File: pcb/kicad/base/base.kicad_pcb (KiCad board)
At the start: 2 copper layers, 45 parts, among them P1 J-Link SWD, P2 SMA, P3 Power Source, P4 USB Micro B, Q1 IRLML2502, U1 SAMB11G18A-edit, U2 XBee-PRO_900HP, Y1 32.768kHz, Y2 26MHz

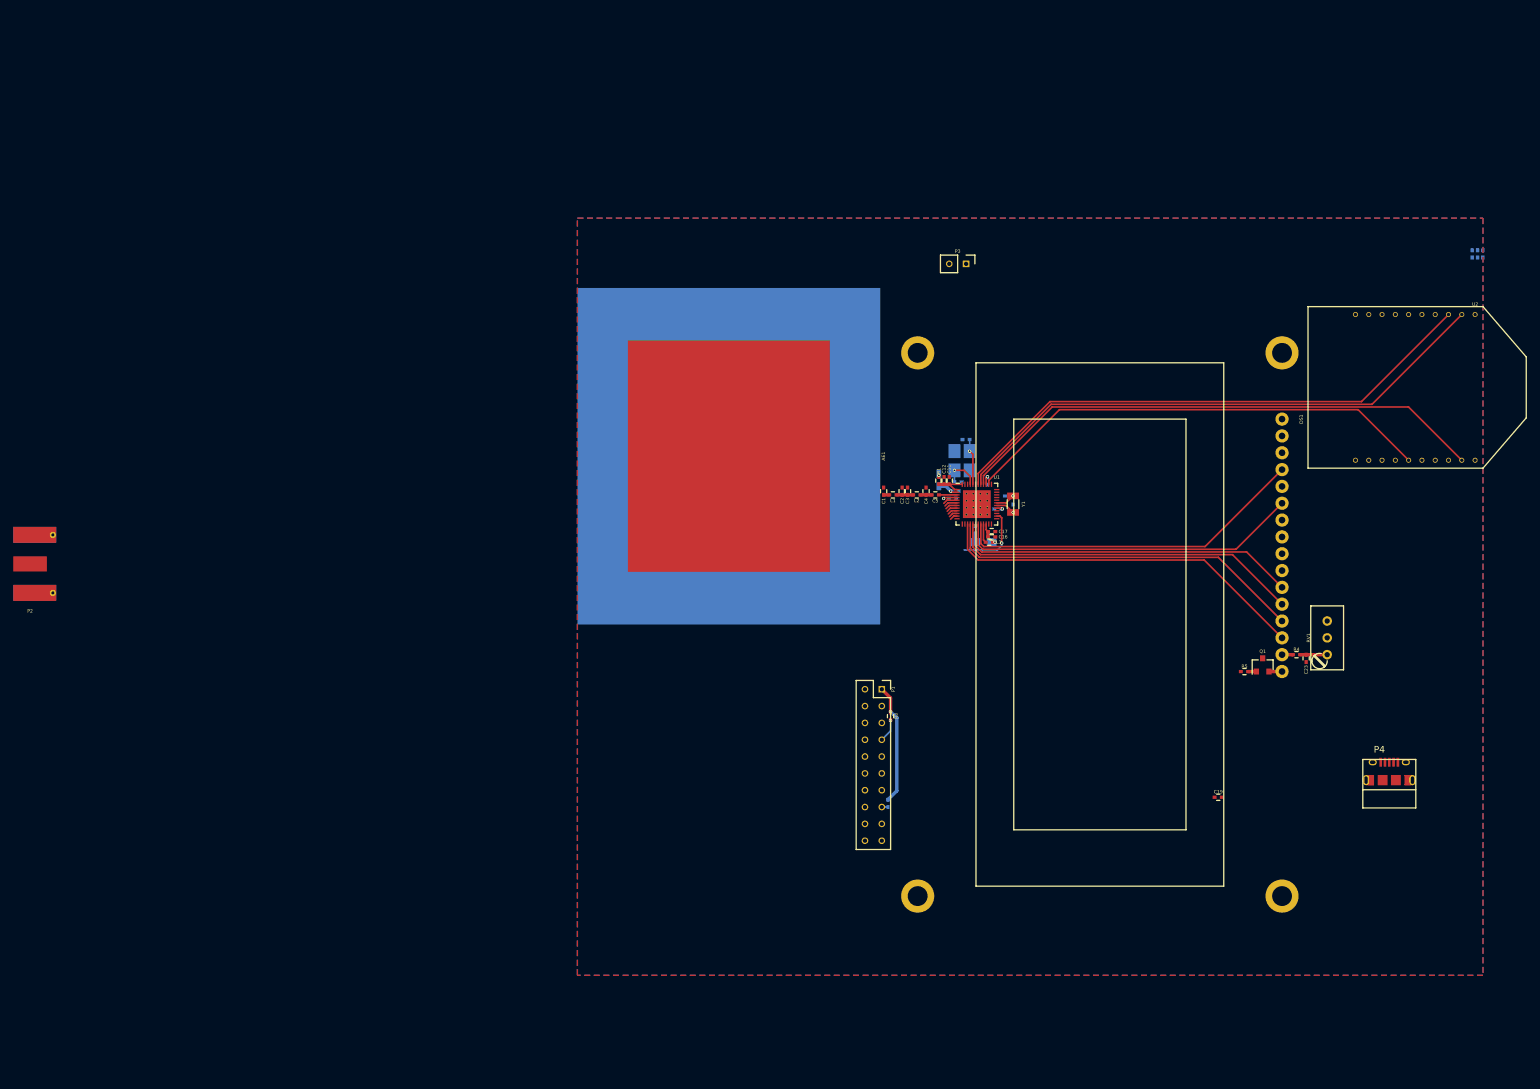
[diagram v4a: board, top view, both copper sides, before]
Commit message: Update display and XBee position once more
GPIO pins were rearranged to achieve a tighter fit on the available
components. Patch antenna is now replaced with SMA connector for first
prototype. Buttons will be simulated with a pin header short. Audio
speaker is planned to go below the display, perhpas on the side of the
housing.
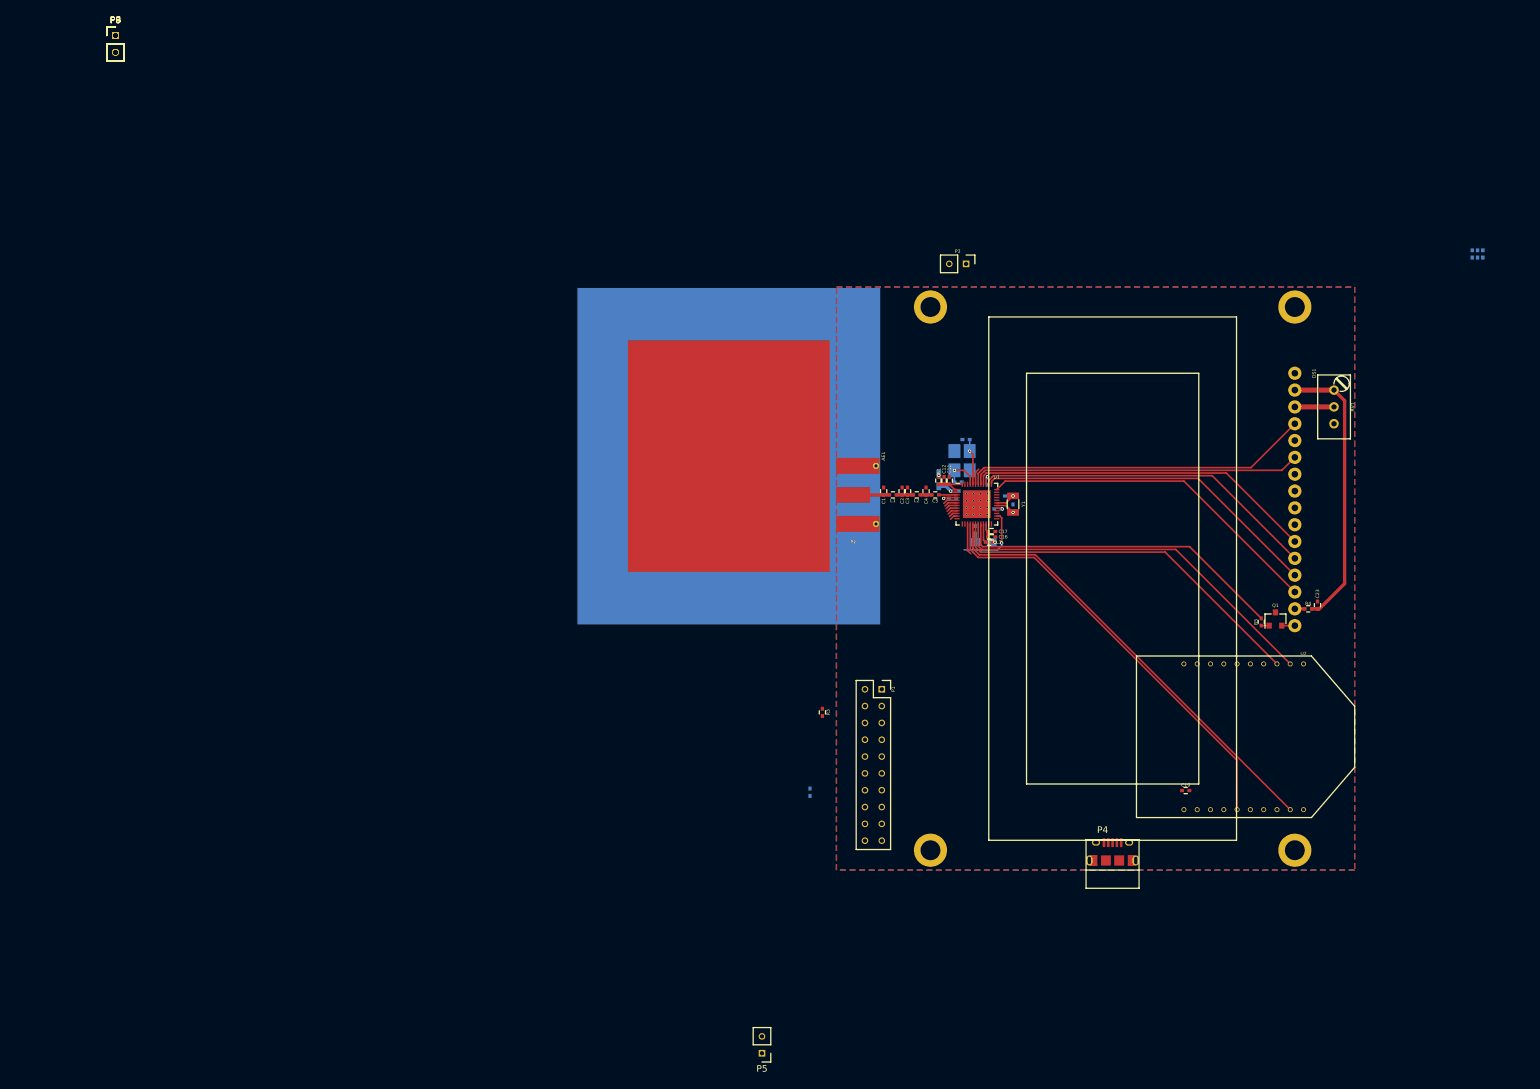
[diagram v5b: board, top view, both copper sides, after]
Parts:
- added P5: Button, Misc:Socket_Strip_Straight_1x02_Pitch2.54mm_Drill0.64mm, F.Cu at (97.6, 153.6)
- added P6, P7, P8, P9: Button, Misc:Socket_Strip_Straight_1x02_Pitch2.54mm_Drill0.64mm, F.Cu at (0.00, 0.00)
- moved P2 124.7 mm to (113.1, 69.3)
- moved U2 58.8 mm to (176.9, 105.9)
- moved P4 43.5 mm to (150.5, 124.5)
- moved RV1 40.0 mm to (183.9, 53.5), turned to 90 degrees
- moved R2 11.9 mm to (104.8, 114.2)
- moved R3 10.3 mm to (106.7, 102.2)
- moved C23 8.21 mm to (181.4, 86.0), turned to 270 degrees
- moved R5 7.91 mm to (172.9, 88.5), turned to 270 degrees
- moved Q1 7.20 mm to (175.1, 88.1)
- moved DS1 7.19 mm to (150.5, 82.0)
- moved R4 7.15 mm to (180.0, 86.5)
- moved C19 5.02 mm to (161.5, 114.0)
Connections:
- AE1 pad 1: /SIG_2.4G -> Net-(AE1-Pad1)
- P2 pad 1: Net-(P2-Pad1) -> /SIG_2.4G
- R5 pad 1: /base-display/BRIGHT -> /DISP_BRIGHT
- U1 pad 10: Net-(U1-Pad10) -> /BTN_UP
- U1 pad 11: Net-(U1-Pad11) -> /BTN_RIGHT
- U1 pad 12: Net-(U1-Pad12) -> /BTN_HELP
- U1 pad 13: Net-(U1-Pad13) -> /Data-
- U1 pad 14: /DISP_CTRST -> /Data+
- U1 pad 15: /DISP_B3 -> /AUDIO_SIG
- U1 pad 16: /DISP_B2 -> /UART_RTS
- U1 pad 17: /DISP_B1 -> /UART_CTS
- U1 pad 18: /DISP_B0 -> /UART_TX
- U1 pad 19: /DISP_E -> /UART_RX
- U1 pad 20: /DISP_REG -> /DISP_BRIGHT
- U1 pad 24: GND -> Net-(U1-Pad24)
- U1 pad 25: GND -> Net-(U1-Pad25)
- U1 pad 27: GND -> Net-(U1-Pad27)
- U1 pad 28: GND -> Net-(U1-Pad28)
- U1 pad 33: GND -> Net-(U1-Pad33)
- U1 pad 36: GND -> /DISP_B3
- U1 pad 37: GND -> /DISP_B2
- U1 pad 38: /UART_RTS -> /DISP_B1
- U1 pad 40: /UART_CTS -> /DISP_B0
- U1 pad 41: /UART_RX -> /DISP_E
- U1 pad 42: /UART_TX -> /DISP_REG
- U1 pad 43: GND -> /DISP_CTRST
- U1 pad 7: /Data- -> Net-(U1-Pad7)
- U1 pad 8: /Data+ -> /BTN_LEFT
- U1 pad 9: Net-(U1-Pad9) -> /BTN_DOWN
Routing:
- net /DISP_BRIGHT: track 0.00 -> 50.1 mm
- net /+5V: track 4.09 -> 42.3 mm
- net /UART_RX: track 84.1 -> 57.8 mm
- net /UART_TX: track 82.6 -> 56.3 mm
- net /+3.3V: track 21.5 -> 3.28 mm, vias 2 -> 1
- net /UART_CTS: track 81.1 -> 67.9 mm
- net /UART_RTS: track 71.5 -> 64.7 mm
- net Net-(DS1-Pad3): track 0.00 -> 5.91 mm
- net /AUDIO_SIG: track 0.00 -> 4.66 mm
- net /SIG_2.4G: track 0.85 -> 5.44 mm
- net /DISP_B3: track 56.8 -> 52.5 mm
- net /SWDIO: track 5.45 -> 2.01 mm, vias 1 -> 0
- net /DISP_B2: track 55.3 -> 52.5 mm
- net /DISP_CTRST: track 0.00 -> 2.46 mm
- net /DISP_E: track 52.1 -> 50.0 mm
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
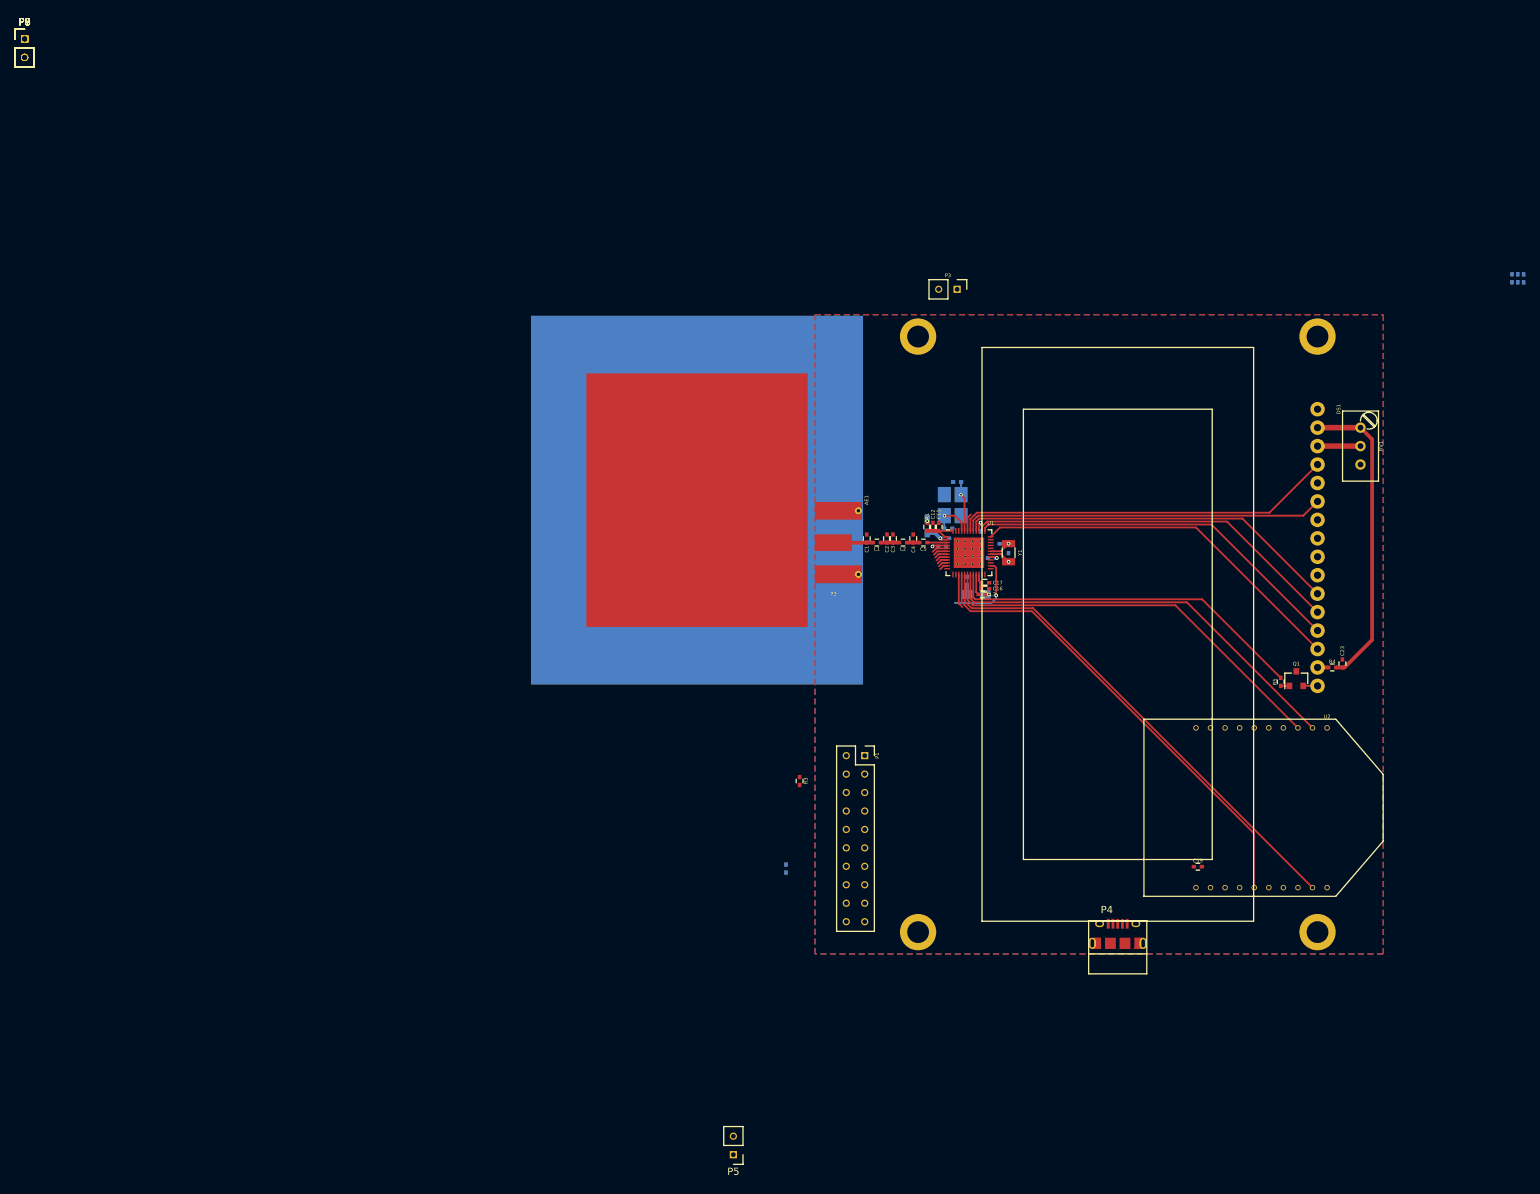
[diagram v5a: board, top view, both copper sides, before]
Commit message: Add power traces throughout board
Power is almost fully distributed to the entire board. All signal traces
have been connected. Copper pours still need to removed from the
RF region. The ferrite bead should also be moved.
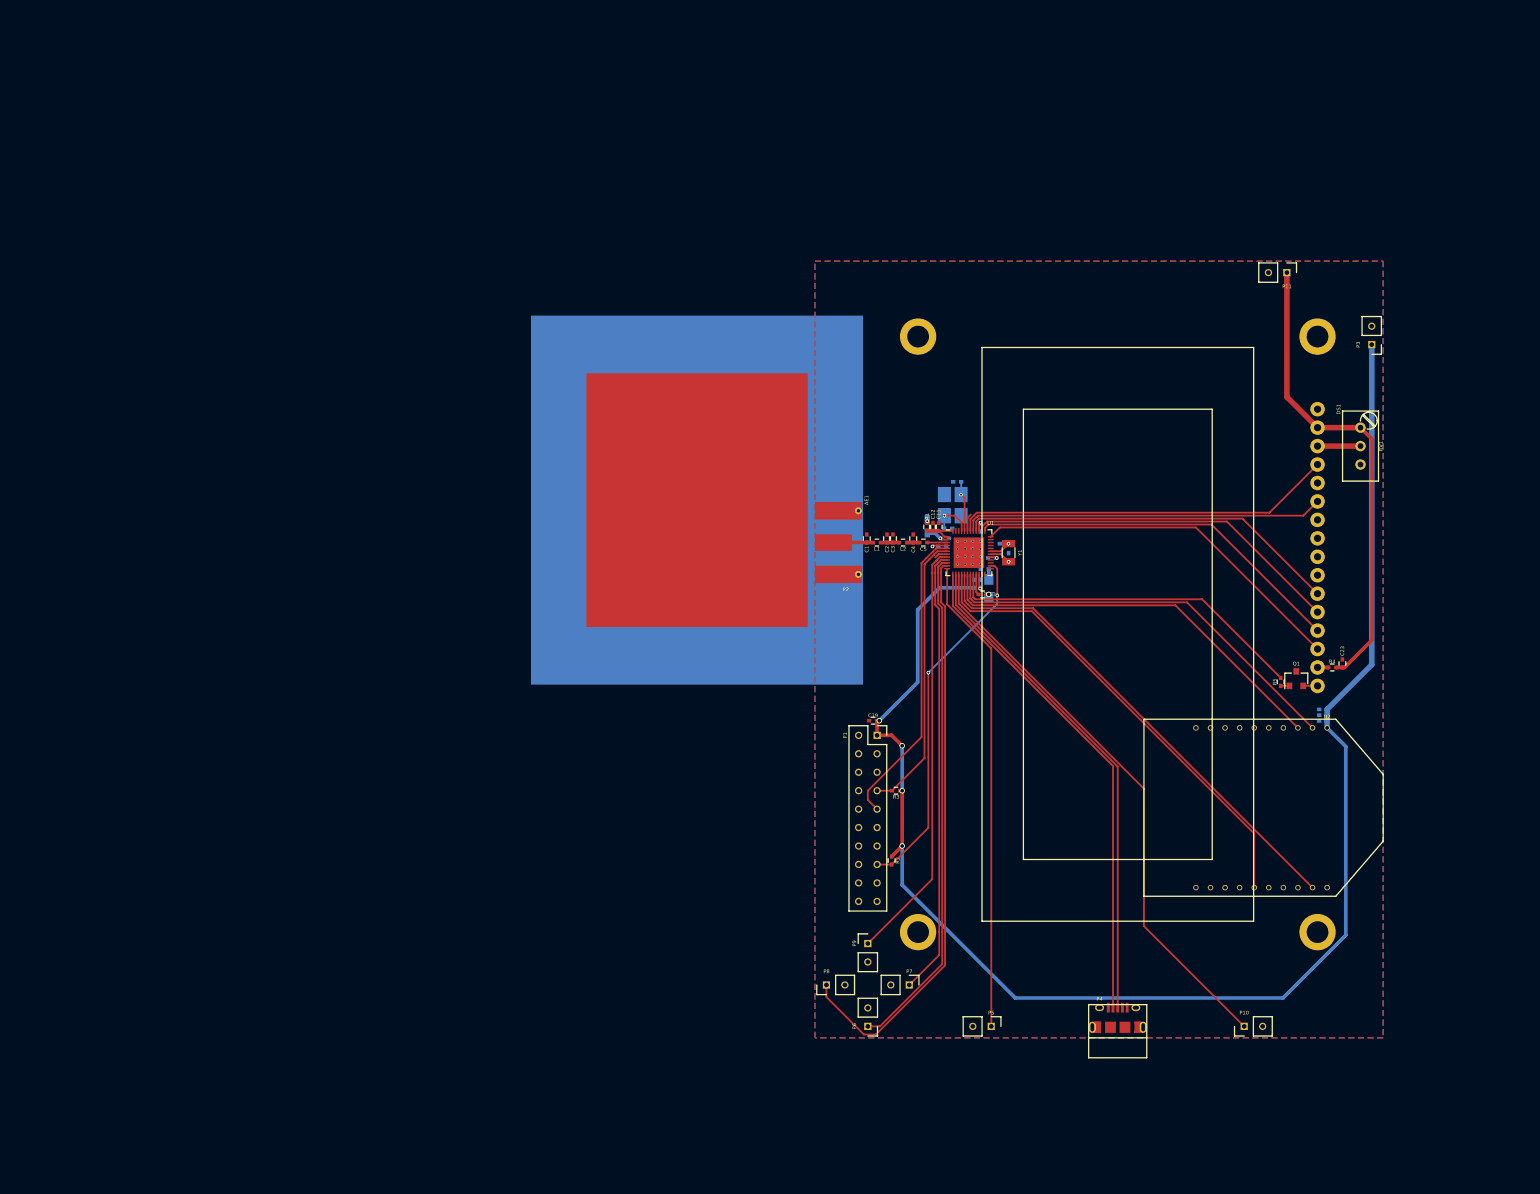
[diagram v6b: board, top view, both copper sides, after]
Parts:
- added P10: CONN_01X02, Misc:Socket_Strip_Straight_1x02_Pitch2.54mm_Drill0.64mm, F.Cu at (167.9, 136.0)
- added P11: CONN_01X02, Misc:Socket_Strip_Straight_1x02_Pitch2.54mm_Drill0.64mm, F.Cu at (173.8, 32.2)
- C16, C17: moved to B.Cu
- P3: value Power Source -> CONN_01X02
- R2: moved to F.Cu
- moved P6 178.8 mm to (116.1, 136.0), turned to 180 degrees
- moved P7 178.3 mm to (121.8, 130.3), turned to 270 degrees
- moved P8 170.7 mm to (110.4, 130.3), turned to 90 degrees
- moved P9 170.3 mm to (116.1, 124.5)
- moved C20 66.3 mm to (178.8, 93.9), turned to 180 degrees
- moved C21 65.9 mm to (178.8, 93.1), turned to 180 degrees
- moved C22 65.5 mm to (178.8, 92.3), turned to 180 degrees
- moved P3 57.6 mm to (185.5, 42.1), turned to 180 degrees
- moved C19 49.0 mm to (116.8, 93.9), turned to 180 degrees
- moved P5 39.7 mm to (133.1, 136.0), turned to 270 degrees
- moved R2 14.6 mm to (119.4, 113.1)
- moved R3 13.3 mm to (120.0, 103.5), turned to 180 degrees
- moved P4 11.6 mm to (150.5, 136.1)
- moved P1 3.27 mm to (117.4, 95.9)
- moved C14 2.92 mm to (132.2, 73.0), turned to 180 degrees
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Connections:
- P5 pad 2: /+3.3V -> GND
- P6 pad 2: /+3.3V -> GND
- P7 pad 2: /+3.3V -> GND
- P8 pad 2: /+3.3V -> GND
- P9 pad 2: /+3.3V -> GND
- U1 pad 10: /BTN_UP -> /BTN_RIGHT
- U1 pad 11: /BTN_RIGHT -> /BTN_DOWN
- U1 pad 9: /BTN_DOWN -> /BTN_UP
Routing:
- net /+3.3V: track 3.28 -> 213.4 mm, vias 1 -> 6
- net /BTN_DOWN: track 1.50 -> 80.0 mm
- net /AUDIO_SIG: track 4.66 -> 78.5 mm
- net /BTN_RIGHT: track 1.16 -> 70.2 mm
- net /Data+: track 0.00 -> 68.9 mm
- net /Data-: track 0.00 -> 68.8 mm
- net /BTN_HELP: track 0.00 -> 65.5 mm
- net /BTN_UP: track 1.32 -> 61.6 mm
- net /BTN_LEFT: track 1.66 -> 58.3 mm
- net /SWDCLK: track 2.19 -> 41.8 mm
- net Net-(P1-Pad15): track 11.0 -> 49.8 mm, vias 1 -> 2
- net /SWDIO: track 2.01 -> 39.0 mm
- net /+5V: track 42.3 -> 65.4 mm

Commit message: Cleanup unconnnected nets and RF region
All remaining power traces have been connected, and copper voids have
been added around the SMA.
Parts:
- added REF**: Via_Stitch_Dia0.356mm_Drill0.254mm, Misc:Via_Stitch_Dia0.356mm_Drill0.254mm, F.Cu at (117.3, 68.2)
- added REF**: Via_Stitch_Dia0.356mm_Drill0.254mm, Misc:Via_Stitch_Dia0.356mm_Drill0.254mm, F.Cu at (117.9, 68.2)
- added REF**: Via_Stitch_Dia0.356mm_Drill0.254mm, Misc:Via_Stitch_Dia0.356mm_Drill0.254mm, F.Cu at (116.8, 68.2)
- added REF**: Via_Stitch_Dia0.356mm_Drill0.254mm, Misc:Via_Stitch_Dia0.356mm_Drill0.254mm, F.Cu at (121.0, 68.1)
- added REF**: Via_Stitch_Dia0.356mm_Drill0.254mm, Misc:Via_Stitch_Dia0.356mm_Drill0.254mm, F.Cu at (121.5, 68.1)
- added REF**: Via_Stitch_Dia0.356mm_Drill0.254mm, Misc:Via_Stitch_Dia0.356mm_Drill0.254mm, F.Cu at (120.4, 68.1)
- moved C14 2.03 mm to (134.0, 73.9), turned to 90 degrees
- moved FB1 1.99 mm to (124.3, 65.1)
- moved C10 0.67 mm to (125.7, 69.9)
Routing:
- net /+3.3V: track 213.4 -> 296.3 mm, vias 6 -> 7
- net Net-(C14-Pad1): track 1.64 -> 45.1 mm, vias 1 -> 6
- net Net-(C10-Pad1): track 7.12 -> 9.21 mm, vias 1 -> 2
- net Net-(C13-Pad1): track 3.12 -> 4.49 mm
- net GND: track 0.00 -> 1.23 mm, vias 0 -> 4
